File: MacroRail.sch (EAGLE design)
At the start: 11 parts, among them CN1 1X4-3.5MM, T1 2N2222, U1 ESP32DEVKITC, U2 TCM2209-V1.2

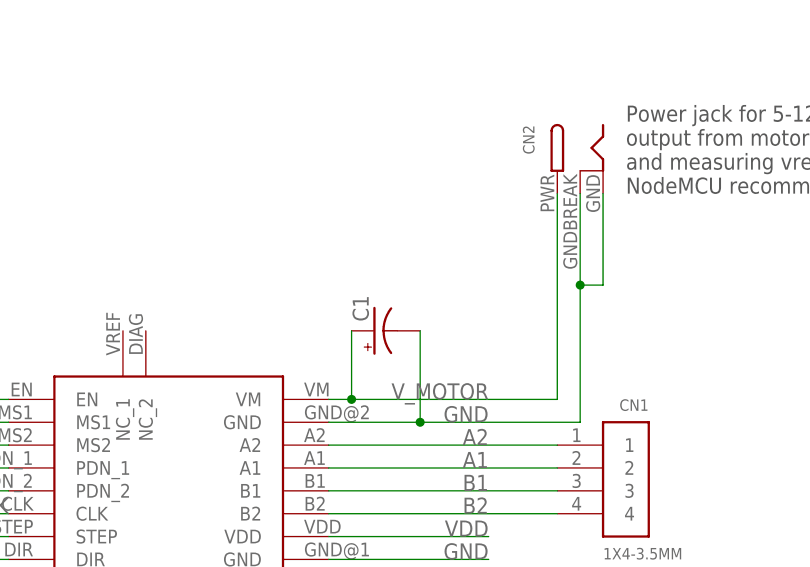
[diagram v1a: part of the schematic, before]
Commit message: Adding basic BOM to README
Adding Bill of Materials and links to example Aliexpress listings.
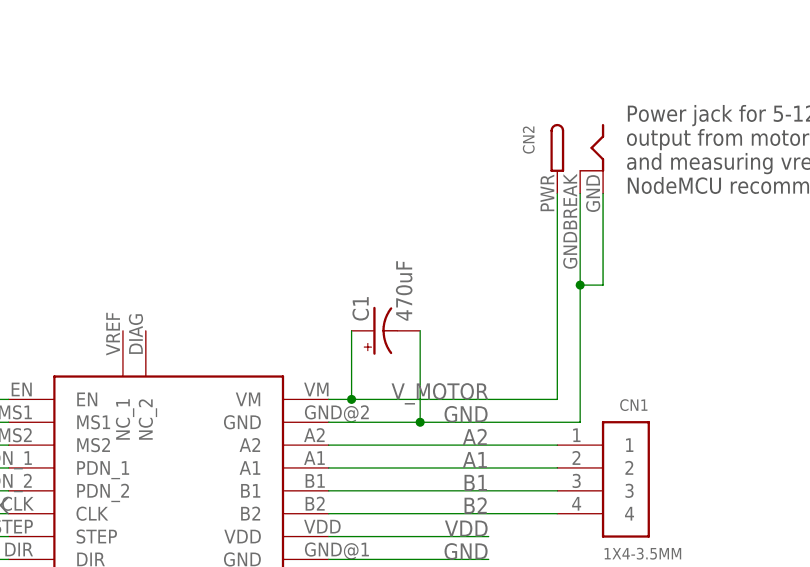
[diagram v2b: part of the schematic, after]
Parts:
- C1: value (none) -> 470uF
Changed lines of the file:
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@@
 <part name="U1" library="ESP32-DEVKITC" deviceset="ESP32DEVKITC" device="" override_package3d_urn="urn:adsk.eagle:package:34287540/2" override_package_urn="urn:adsk.eagle:footprint:34287541/1"/>
 <part name="U2" library="00-Random-Components-Simen" library_urn="urn:adsk.eagle:library:24319138" deviceset="TCM2209-V1.2" device="" package3d_urn="urn:adsk.eagle:package:34261111/3" override_package3d_urn="urn:adsk.eagle:package:34287606/2" override_package_urn="urn:adsk.eagle:footprint:34261109/3"/>
-<part name="C1" library="rcl" library_urn="urn:adsk.eagle:library:334" deviceset="CPOL-US" device="E5-8.5" package3d_urn="urn:adsk.eagle:package:23374/1" override_package3d_urn="urn:adsk.eagle:package:34287653/3" override_package_urn="urn:adsk.eagle:footprint:22875/1"/>
+<part name="C1" library="rcl" library_urn="urn:adsk.eagle:library:334" deviceset="CPOL-US" device="E5-8.5" package3d_urn="urn:adsk.eagle:package:23374/1" override_package3d_urn="urn:adsk.eagle:package:34287653/3" override_package_urn="urn:adsk.eagle:footprint:22875/1" value="470uF"/>
 <part name="R1" library="rcl" library_urn="urn:adsk.eagle:library:334" deviceset="R-US_" device="0207/7" package3d_urn="urn:adsk.eagle:package:23493/2" value="1k"/>
 <part name="T1" library="adafruit" library_urn="urn:adsk.eagle:library:420" deviceset="2N2222" device="" package3d_urn="urn:adsk.eagle:package:6240647/1" override_package3d_urn="urn:adsk.eagle:package:34287641/2" override_package_urn="urn:adsk.eagle:footprint:6240001/1"/>

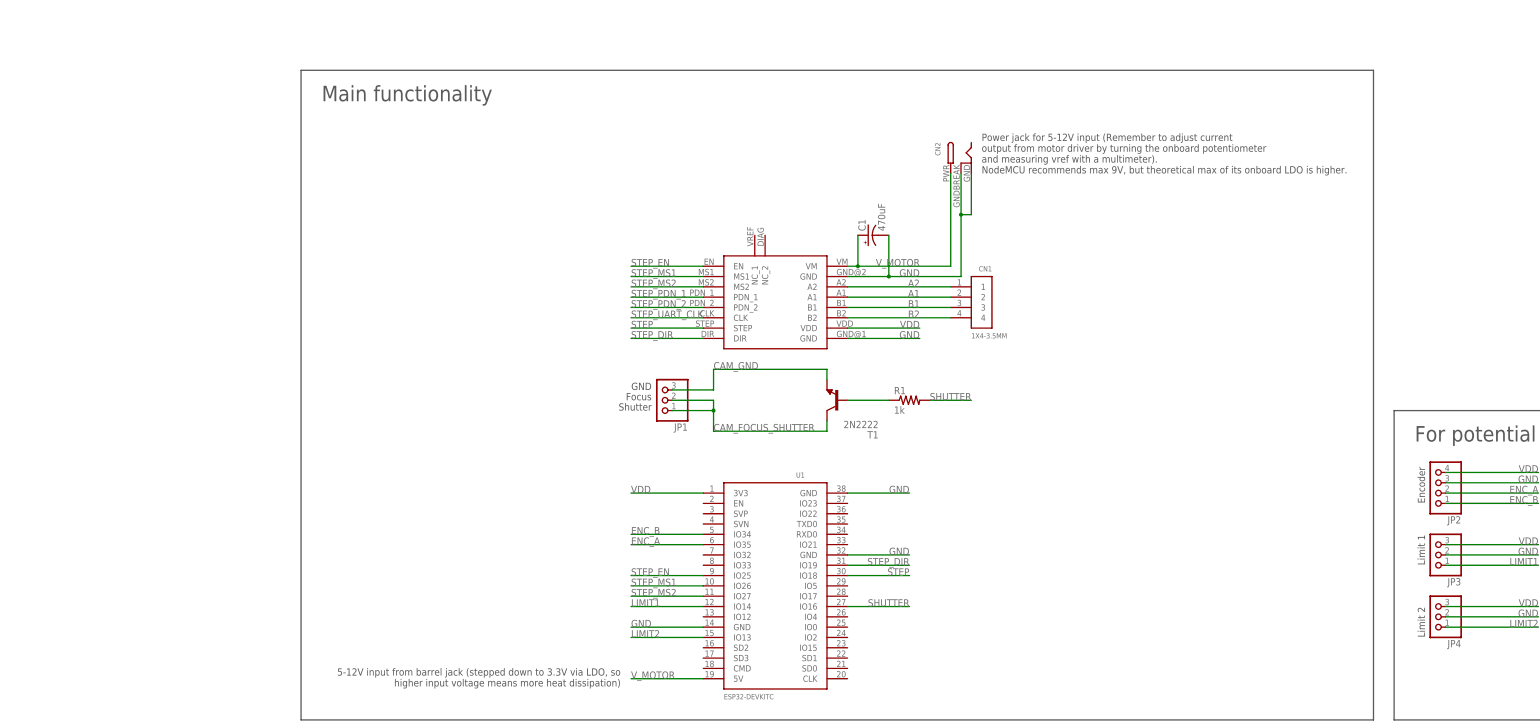
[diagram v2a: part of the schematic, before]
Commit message: Redesigned shutter circuit
Complete redesign of the shutter circuit to make it more flexible and camera agnostic. The user will have to modify the board to match with what their camera expects.
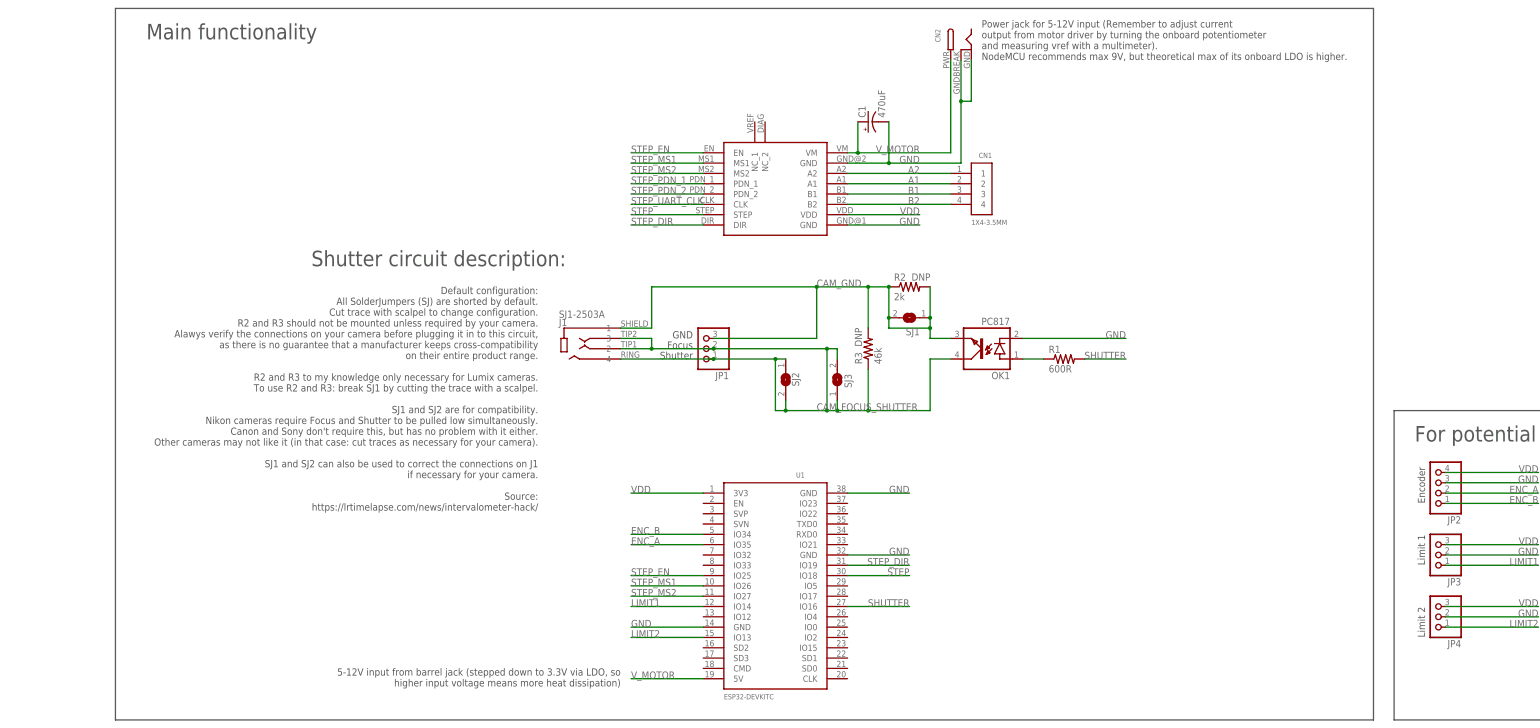
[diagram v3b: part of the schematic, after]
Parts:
- removed T1: 2N2222, adafruit:2N2222
- added J1: SJ1-2503A, 00-Random-Components-Simen:SJ1-2503A
- added OK1: PC817, optocoupler:PC817
- added R2: 2k, rcl:R-US_0207/7
- added R3: 46k, rcl:R-US_0207/7
- added SJ1, SJ2, SJ3: (no value), jumper:SJ
- R1: value 1k -> 600R
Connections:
- removed net N$3: R1.1, T1.B
- new net N$1: OK1.A, R1.1
- net CAM_FOCUS_SHUTTER: now also J1.2, J1.3, J1.4, OK1.COL, R3.1, SJ2.1, SJ2.2, SJ3.1, SJ3.2; no longer T1.C
- net CAM_GND: now also J1.1, OK1.EMIT, R2.1, R2.2, R3.2, SJ1.1, SJ1.2; no longer T1.E
- net GND: now also OK1.C
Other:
- note added: "Default configuration: All SolderJumpers (SJ) are shorted by default. Cut trace with scalpel to change configuration. R2 and R3 should not be mounted unless required by your camera. Alawys verify the connections on your camera before plugging it in to this circuit, as there is no guarantee that a manufacturer keeps cross-compatibility on their entire product range. R2 and R3 to my knowledge only 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"
- note added: "Shutter circuit description:"
- moved on the sheet: C1, CN1, CN2, JP1, R1

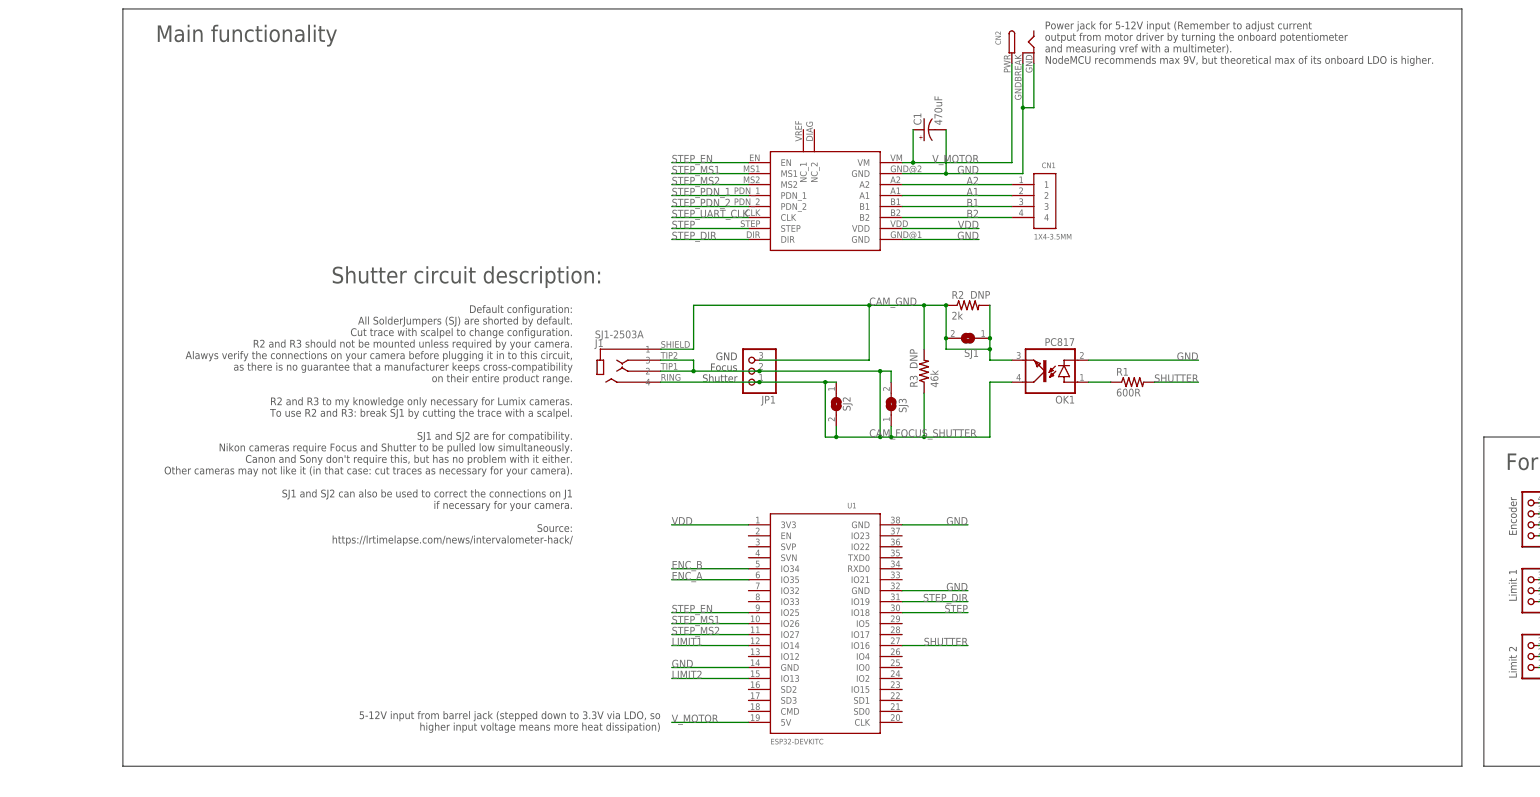
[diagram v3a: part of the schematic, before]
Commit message: V1.0
Redesigned power planes and added more documentation in silk screen.
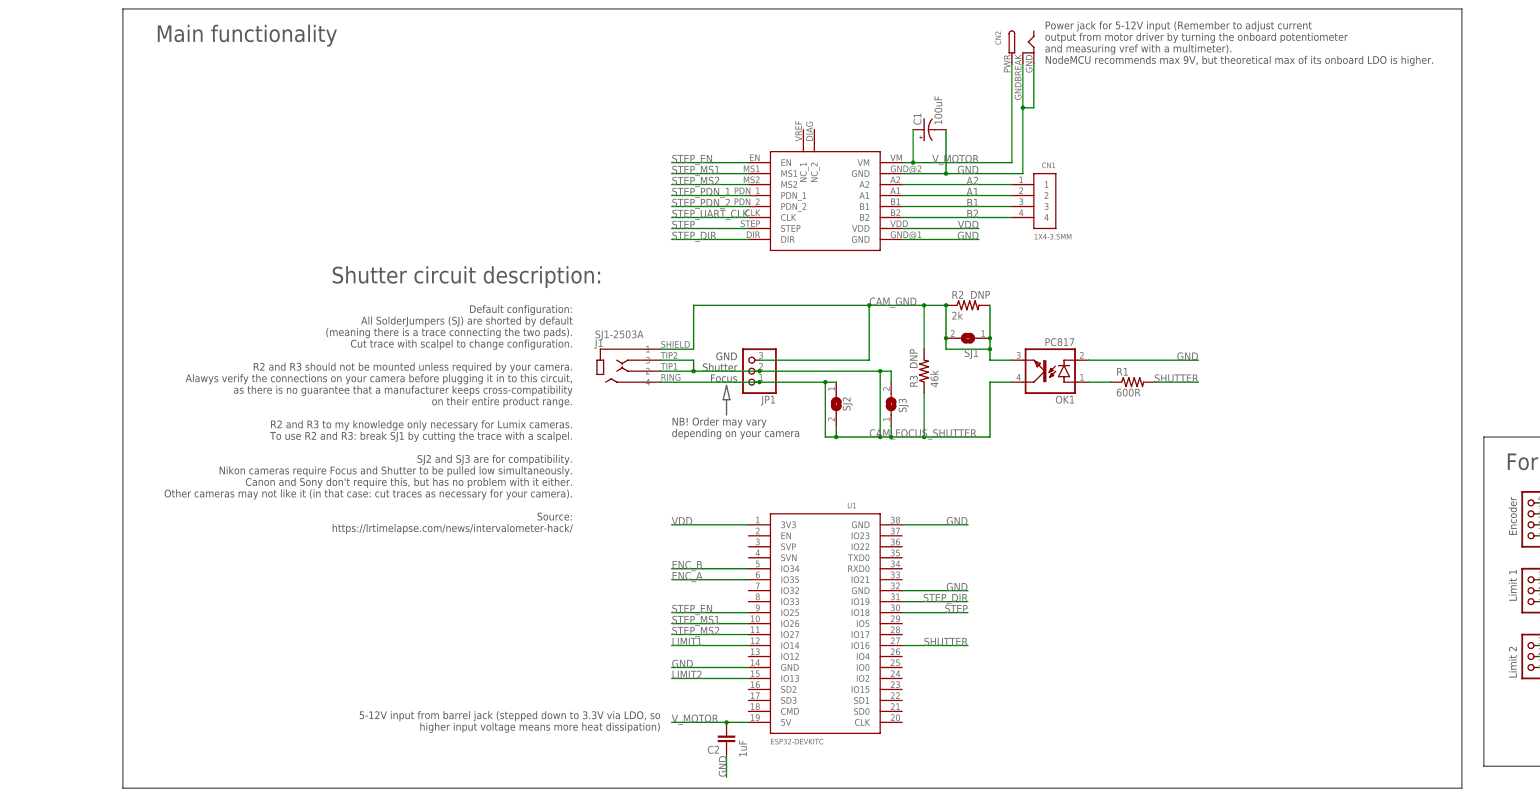
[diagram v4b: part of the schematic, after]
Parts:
- added C2: 1uF, rcl:C-EU050-024X044
- C1: value 470uF -> 100uF
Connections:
- net GND: now also C2.1
- net V_MOTOR: now also C2.2
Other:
- note added: "Default configuration: All SolderJumpers (SJ) are shorted by default (meaning there is a trace connecting the two pads). Cut trace with scalpel to change configuration. R2 and R3 should not be mounted unless required by your camera. Alawys verify the connections on your camera before plugging it in to this circuit, as there is no guarantee that a manufacturer keeps cross-compatibility on their en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"
- note added: "NB! Order may vary depending on your camera"
- note removed: "Default configuration: All SolderJumpers (SJ) are shorted by default. Cut trace with scalpel to change configuration. R2 and R3 should not be mounted unless required by your camera. Alawys verify the connections on your camera before plugging it in to this circuit, as there is no guarantee that a manufacturer keeps cross-compatibility on their entire product range. R2 and R3 to my knowledge only 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"
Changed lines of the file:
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@@
 <class number="0" name="default" width="0" drill="0">
+</class>
+<class number="1" name="PWR" width="1.27" drill="0">
 </class>
 </classes>
@@
 <part name="U1" library="ESP32-DEVKITC" deviceset="ESP32DEVKITC" device="" override_package3d_urn="urn:adsk.eagle:package:34287540/2" override_package_urn="urn:adsk.eagle:footprint:34287541/1"/>
 <part name="U2" library="00-Random-Components-Simen" library_urn="urn:adsk.eagle:library:24319138" deviceset="TCM2209-V1.2" device="" package3d_urn="urn:adsk.eagle:package:34261111/3" override_package3d_urn="urn:adsk.eagle:package:34287606/2" override_package_urn="urn:adsk.eagle:footprint:34261109/3"/>
-<part name="C1" library="rcl" library_urn="urn:adsk.eagle:library:334" deviceset="CPOL-US" device="E5-8.5" package3d_urn="urn:adsk.eagle:package:23374/1" override_package3d_urn="urn:adsk.eagle:package:34287653/3" override_package_urn="urn:adsk.eagle:footprint:22875/1" value="470uF"/>
+<part name="C1" library="rcl" library_urn="urn:adsk.eagle:library:334" deviceset="CPOL-US" device="E5-8.5" package3d_urn="urn:adsk.eagle:package:23374/1" override_package3d_urn="urn:adsk.eagle:package:34287653/3" override_package_urn="urn:adsk.eagle:footprint:22875/1" value="100uF"/>
 <part name="R1" library="rcl" library_urn="urn:adsk.eagle:library:334" deviceset="R-US_" device="0207/7" package3d_urn="urn:adsk.eagle:package:23493/2" value="600R"/>
 <part name="CN1" library="adafruit" library_urn="urn:adsk.eagle:library:420" deviceset="1X4" device="-3.5MM" package3d_urn="urn:adsk.eagle:package:6240819/1" override_package3d_urn="urn:adsk.eagle:package:34287611/2" override_package_urn="urn:adsk.eagle:footprint:6240174/1"/>
@@
 <part name="SJ1" library="jumper" library_urn="urn:adsk.eagle:library:252" deviceset="SJ" device="" package3d_urn="urn:adsk.eagle:package:15471/1"/>
 <part name="J1" library="00-Random-Components-Simen" library_urn="urn:adsk.eagle:library:24319138" deviceset="SJ1-2503A" device="" package3d_urn="urn:adsk.eagle:package:34317647/3" override_package3d_urn="urn:adsk.eagle:package:34319661/2" override_package_urn="urn:adsk.eagle:footprint:34317645/1" override_locally_modified="yes"/>
+<part name="C2" library="rcl" library_urn="urn:adsk.eagle:library:334" deviceset="C-EU" device="050-024X044" package3d_urn="urn:adsk.eagle:package:23643/1" override_package3d_urn="urn:adsk.eagle:package:34322317/2" override_package_urn="urn:adsk.eagle:footprint:23147/1" value="1uF"/>
 </parts>
 <sheets>
@@
 <plain>
 <text x="-17.78" y="96.52" size="1.778" layer="97" rot="MR0">GND</text>
-<text x="-17.78" y="93.98" size="1.778" layer="97" rot="MR0">Focus</text>
-<text x="-17.78" y="91.44" size="1.778" layer="97" rot="MR0">Shutter</text>
+<text x="-17.78" y="91.44" size="1.778" layer="97" rot="MR0">Focus</text>
+<text x="-17.78" y="93.98" size="1.778" layer="97" rot="MR0">Shutter</text>
 <text x="53.34" y="165.1" size="1.778" layer="97">Power jack for 5-12V input (Remember to adjust current
 output from motor driver by turning the onboard potentiometer
@@
 <text x="-152.4" y="170.18" size="3.81" layer="97">Main functionality</text>
 <wire x1="-160.02" y1="177.8" x2="149.86" y2="177.8" width="0.1524" layer="97"/>
-<wire x1="149.86" y1="177.8" x2="149.86" y2="2.54" width="0.1524" layer="97"/>
-<wire x1="149.86" y1="2.54" x2="-160.02" y2="2.54" width="0.1524" layer="97"/>
-<wire x1="-160.02" y1="2.54" x2="-160.02" y2="177.8" width="0.1524" layer="97"/>
+<wire x1="149.86" y1="177.8" x2="149.86" y2="-2.54" width="0.1524" layer="97"/>
+<wire x1="149.86" y1="-2.54" x2="-160.02" y2="-2.54" width="0.1524" layer="97"/>
+<wire x1="-160.02" y1="-2.54" x2="-160.02" y2="177.8" width="0.1524" layer="97"/>
 <text x="-55.88" y="109.22" size="1.778" layer="97" rot="MR180" align="bottom-right">Default configuration:
-All SolderJumpers (SJ) are shorted by default.
+All SolderJumpers (SJ) are shorted by default
+(meaning there is a trace connecting the two pads).
 Cut trace with scalpel to change configuration.
 R2 and R3 should not be mounted unless required by your camera.
@@
 R2 and R3 to my knowledge only necessary for Lumix cameras.
 To use R2 and R3: break SJ1 by cutting the trace with a scalpel.
-SJ1 and SJ2 are for compatibility.
+SJ2 and SJ3 are for compatibility.
 Nikon cameras require Focus and Shutter to be pulled low simultaneously.
 Canon and Sony don't require this, but has no problem with it either.
 Other cameras may not like it (in that case: cut traces as necessary for your camera).
-SJ1 and SJ2 can also be used to correct the connections on J1
-if necessary for your camera.
 Source:
 https://lrtimelapse.com/news/intervalometer-hack/</text>
 <text x="-111.76" y="114.3" size="3.81" layer="97">Shutter circuit description:</text>
+<text x="-33.02" y="78.74" size="1.778" layer="97">NB! Order may vary
+depending on your camera</text>
+<wire x1="-20.32" y1="90.678" x2="-19.558" y2="87.376" width="0.1524" layer="97"/>
+<wire x1="-19.558" y1="87.376" x2="-20.32" y2="87.376" width="0.1524" layer="97"/>
+<wire x1="-20.32" y1="87.376" x2="-21.082" y2="87.376" width="0.1524" layer="97"/>
+<wire x1="-21.082" y1="87.376" x2="-20.32" y2="90.678" width="0.1524" layer="97"/>
+<wire x1="-20.32" y1="83.82" x2="-20.32" y2="87.376" width="0.1524" layer="97"/>
 </plain>
 <instances>
@@
 <attribute name="NAME" x="-50.8" y="99.568" size="1.778" layer="95" font="vector"/>
 <attribute name="VALUE" x="-50.8" y="101.6" size="1.778" layer="96" font="vector"/>
+</instance>
+<instance part="C2" gate="G$1" x="-20.32" y="7.62" smashed="yes" rot="R180">
+<attribute name="NAME" x="-21.844" y="7.239" size="1.778" layer="95" rot="R180"/>
+<attribute name="VALUE" x="-17.399" y="8.636" size="1.778" layer="96" rot="R270"/>
 </instance>
 </instances>
@@
 </segment>
 </net>
-<net name="V_MOTOR" class="0">
+<net name="V_MOTOR" class="1">
 <segment>
 <pinref part="U2" gate="G$1" pin="VM"/>
@@
 <segment>
 <pinref part="U1" gate="G$1" pin="5V"/>
-<wire x1="-15.24" y1="12.7" x2="-33.02" y2="12.7" width="0.1524" layer="91"/>
+<wire x1="-15.24" y1="12.7" x2="-20.32" y2="12.7" width="0.1524" layer="91"/>
 <label x="-33.02" y="12.7" size="1.778" layer="95"/>
-</segment>
-</net>
-<net name="GND" class="0">
+<pinref part="C2" gate="G$1" pin="2"/>
+<wire x1="-20.32" y1="12.7" x2="-33.02" y2="12.7" width="0.1524" layer="91"/>
+<junction x="-20.32" y="12.7"/>
+</segment>
+</net>
+<net name="GND" class="1">
 <segment>
 <pinref part="U2" gate="G$1" pin="GND@1"/>
@@
 <label x="88.9" y="96.52" size="1.778" layer="95" rot="MR0"/>
 </segment>
-</net>
-<net name="A2" class="0">
+<segment>
+<pinref part="C2" gate="G$1" pin="1"/>
+<wire x1="-20.32" y1="5.08" x2="-20.32" y2="0" width="0.1524" layer="91"/>
+<label x="-20.32" y="0" size="1.778" layer="95" rot="R90"/>
+</segment>
+</net>
+<net name="A2" class="1">
 <segment>
 <pinref part="U2" gate="G$1" pin="A2"/>
@@
 </segment>
 </net>
-<net name="A1" class="0">
+<net name="A1" class="1">
 <segment>
 <pinref part="CN1" gate="G$1" pin="2"/>
@@
 </segment>
 </net>
-<net name="B1" class="0">
+<net name="B1" class="1">
 <segment>
 <pinref part="U2" gate="G$1" pin="B1"/>
@@
 </segment>
 </net>
-<net name="B2" class="0">
+<net name="B2" class="1">
 <segment>
 <pinref part="CN1" gate="G$1" pin="4"/>
@@
 </segment>
 </net>
-<net name="VDD" class="0">
+<net name="VDD" class="1">
 <segment>
 <pinref part="U2" gate="G$1" pin="VDD"/>
